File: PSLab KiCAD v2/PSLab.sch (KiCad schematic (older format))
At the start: 69 parts, among them CON1 USB-MINI-B, P10 Analog, P12 5V, P13 MCLR, P2 PROG, P3 DIO, P4 V+/V-, P5 sen-cap, P6 I2C, P7 NRF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

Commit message: Merged with Upstream to fix conflicts
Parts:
- added Q2: MMBT3904, TO_SOT_Packages_SMD:SOT-23, symbol MMBT3904
- added Q3: MMBT3906, TO_SOT_Packages_SMD:SOT-23, symbol MMBT3906
- R11, R5: value 200 -> 1K
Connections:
- wire segments 216 -> 228
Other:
- moved on the sheet: D1, D2, R11, R5
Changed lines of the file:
@@
 L R-RESCUE-proto1 R5
 U 1 1 55BABAB3
-P 10450 3000
-F 0 "R5" V 10530 3000 40  0000 C CNN
-F 1 "200" V 10457 3001 40  0000 C CNN
-F 2 "MyLib:R_0805" V 10380 3000 30  0001 C CNN
-F 3 "" H 10450 3000 30  0000 C CNN
-	1    10450 3000
-	0    1    -1   0
+P 10350 2920
+F 0 "R5" V 10430 2920 40  0000 C CNN
+F 1 "1K" V 10357 2921 40  0000 C CNN
+F 2 "MyLib:R_0805" V 10280 2920 30  0001 C CNN
+F 3 "" H 10350 2920 30  0000 C CNN
+	1    10350 2920
+	1    0    0    1
 $EndComp
 $Comp
 L R-RESCUE-proto1 R11
 U 1 1 55BABE2E
-P 10450 4000
-F 0 "R11" V 10530 4000 40  0000 C CNN
-F 1 "200" V 10457 4001 40  0000 C CNN
-F 2 "MyLib:R_0805" V 10380 4000 30  0001 C CNN
-F 3 "" H 10450 4000 30  0000 C CNN
-	1    10450 4000
-	0    1    -1   0
+P 10350 4285
+F 0 "R11" V 10430 4285 40  0000 C CNN
+F 1 "1K" V 10357 4286 40  0000 C CNN
+F 2 "MyLib:R_0805" V 10280 4285 30  0001 C CNN
+F 3 "" H 10350 4285 30  0000 C CNN
+	1    10350 4285
+	1    0    0    1
 $EndComp
 $Comp
 L ZENERsmall-RESCUE-proto1 D1
 U 1 1 55BABFCA
-P 10600 3225
-F 0 "D1" H 10600 3325 40  0000 C CNN
-F 1 "5V6" H 10600 3125 30  0000 C CNN
-F 2 "DIODE:Diode-MiniMELF_Standard" H 10600 3225 60  0001 C CNN
-F 3 "" H 10600 3225 60  0000 C CNN
-	1    10600 3225
-	1    0    0    -1
+P 10550 3360
+F 0 "D1" H 10550 3460 40  0000 C CNN
+F 1 "5V6" H 10550 3260 30  0000 C CNN
+F 2 "DIODE:Diode-MiniMELF_Standard" H 10550 3360 60  0001 C CNN
+F 3 "" H 10550 3360 60  0000 C CNN
+	1    10550 3360
+	0    -1   -1   0
 $EndComp
 $Comp
 L GND-RESCUE-proto1 #PWR046
 U 1 1 55BAC428
-P 10500 3225
-F 0 "#PWR046" H 10500 3225 30  0001 C CNN
-F 1 "GND" H 10500 3155 30  0001 C CNN
-F 2 "" H 10500 3225 60  0000 C CNN
-F 3 "" H 10500 3225 60  0000 C CNN
-	1    10500 3225
-	0    1    1    0
+P 10550 3535
+F 0 "#PWR046" H 10550 3535 30  0001 C CNN
+F 1 "GND" H 10550 3465 30  0001 C CNN
+F 2 "" H 10550 3535 60  0000 C CNN
+F 3 "" H 10550 3535 60  0000 C CNN
+	1    10550 3535
+	1    0    0    -1
 $EndComp
 $Comp
 L ZENERsmall-RESCUE-proto1 D2
 U 1 1 55BACB8F
-P 10600 3750
-F 0 "D2" H 10600 3850 40  0000 C CNN
-F 1 "5V6" H 10600 3650 30  0000 C CNN
-F 2 "DIODE:Diode-MiniMELF_Standard" H 10600 3750 60  0001 C CNN
-F 3 "" H 10600 3750 60  0000 C CNN
-	1    10600 3750
-	-1   0    0    1
+P 10550 3845
+F 0 "D2" H 10550 3945 40  0000 C CNN
+F 1 "5V6" H 10550 3745 30  0000 C CNN
+F 2 "DIODE:Diode-MiniMELF_Standard" H 10550 3845 60  0001 C CNN
+F 3 "" H 10550 3845 60  0000 C CNN
+	1    10550 3845
+	0    -1   -1   0
 $EndComp
 $Comp
 L GND-RESCUE-proto1 #PWR047
 U 1 1 55BACCF3
-P 10500 3750
-F 0 "#PWR047" H 10500 3750 30  0001 C CNN
-F 1 "GND" H 10500 3680 30  0001 C CNN
-F 2 "" H 10500 3750 60  0000 C CNN
-F 3 "" H 10500 3750 60  0000 C CNN
-	1    10500 3750
-	0    1    1    0
-$EndComp
-Text GLabel 10850 4000 2    60   Input ~ 0
+P 10550 3690
+F 0 "#PWR047" H 10550 3690 30  0001 C CNN
+F 1 "GND" H 10550 3620 30  0001 C CNN
+F 2 "" H 10550 3690 60  0000 C CNN
+F 3 "" H 10550 3690 60  0000 C CNN
+	1    10550 3690
+	-1   0    0    1
+$EndComp
+Text GLabel 10875 4705 2    60   Input ~ 0
 VR-
-Text GLabel 10850 3000 2    60   Input ~ 0
+Text GLabel 10885 2580 2    60   Input ~ 0
 VR+
 Text GLabel 4550 7175 0    40   Input ~ 0
@@
 L PWR_FLAG #FLG049
 U 1 1 55BC0DD9
-P 10700 3000
-F 0 "#FLG049" H 10700 3095 30  0001 C CNN
-F 1 "PWR_FLAG" H 10700 3180 30  0000 C CNN
-F 2 "" H 10700 3000 60  0000 C CNN
-F 3 "" H 10700 3000 60  0000 C CNN
-	1    10700 3000
+P 10815 2480
+F 0 "#FLG049" H 10815 2575 30  0001 C CNN
+F 1 "PWR_FLAG" H 10815 2660 30  0000 C CNN
+F 2 "" H 10815 2480 60  0000 C CNN
+F 3 "" H 10815 2480 60  0000 C CNN
+	1    10815 2480
 	1    0    0    -1
 $EndComp
@@
 L PWR_FLAG #FLG050
 U 1 1 55BC113E
-P 10700 4000
-F 0 "#FLG050" H 10700 4095 30  0001 C CNN
-F 1 "PWR_FLAG" H 10700 4180 30  0000 C CNN
-F 2 "" H 10700 4000 60  0000 C CNN
-F 3 "" H 10700 4000 60  0000 C CNN
-	1    10700 4000
+P 10795 4745
+F 0 "#FLG050" H 10795 4840 30  0001 C CNN
+F 1 "PWR_FLAG" H 10795 4925 30  0000 C CNN
+F 2 "" H 10795 4745 60  0000 C CNN
+F 3 "" H 10795 4745 60  0000 C CNN
+	1    10795 4745
 	-1   0    0    1
 $EndComp
@@
 Wire Wire Line
 	6250 4100 7050 4100
-Wire Wire Line
-	10200 3000 9925 3000
 Connection ~ 9925 3000
-Wire Wire Line
-	10200 4000 9925 4000
 Connection ~ 9925 4000
-Wire Wire Line
-	10700 3000 10850 3000
-Wire Wire Line
-	10700 3000 10700 3225
-Wire Wire Line
-	10700 3750 10700 4000
-Wire Wire Line
-	10700 4000 10850 4000
 Wire Wire Line
 	8025 2900 8025 3325
@@
 Wire Wire Line
 	1600 2575 1425 2575
+$Comp
+L MMBT3904 Q2
+U 1 1 593925C9
+P 10550 2680
+F 0 "Q2" V 10775 2515 50  0000 L CNN
+F 1 "MMBT3904" V 10770 2670 50  0000 L CNN
+F 2 "TO_SOT_Packages_SMD:SOT-23" H 10750 2605 50  0001 L CIN
+F 3 "" H 10550 2680 50  0001 L CNN
+	1    10550 2680
+	0    -1   -1   0
+$EndComp
+Wire Wire Line
+	10815 2480 10815 2580
+Wire Wire Line
+	10750 2580 10885 2580
+Connection ~ 10815 2580
+Wire Wire Line
+	10350 2670 10350 2580
+Wire Wire Line
+	10350 2580 10235 2580
+Wire Wire Line
+	10235 2580 10235 3000
+Wire Wire Line
+	10235 3000 9925 3000
+Wire Wire Line
+	10550 2880 10550 3260
+Wire Wire Line
+	10550 3535 10550 3460
+Connection ~ 10550 3240
+Wire Wire Line
+	10350 3170 10350 3240
+Wire Wire Line
+	10350 3240 10550 3240
+Wire Wire Line
+	10550 3745 10550 3690
+Wire Wire Line
+	10350 4035 10350 3995
+Wire Wire Line
+	10350 3995 10550 3995
+Wire Wire Line
+	10550 3945 10550 4405
+$Comp
+L MMBT3906 Q3
+U 1 1 5939854E
+P 10550 4605
+F 0 "Q3" V 10795 4445 50  0000 L CNN
+F 1 "MMBT3906" V 10795 4605 50  0000 L CNN
+F 2 "TO_SOT_Packages_SMD:SOT-23" H 10750 4530 50  0001 L CIN
+F 3 "" H 10550 4605 50  0001 L CNN
+	1    10550 4605
+	0    -1   1    0
+$EndComp
+Wire Wire Line
+	10350 4705 10350 4705
+Wire Wire Line
+	10350 4705 10350 4535
+Connection ~ 10550 3995
+Wire Wire Line
+	10750 4705 10875 4705
+Wire Wire Line
+	10795 4745 10795 4705
+Connection ~ 10795 4705
 $EndSCHEMATC

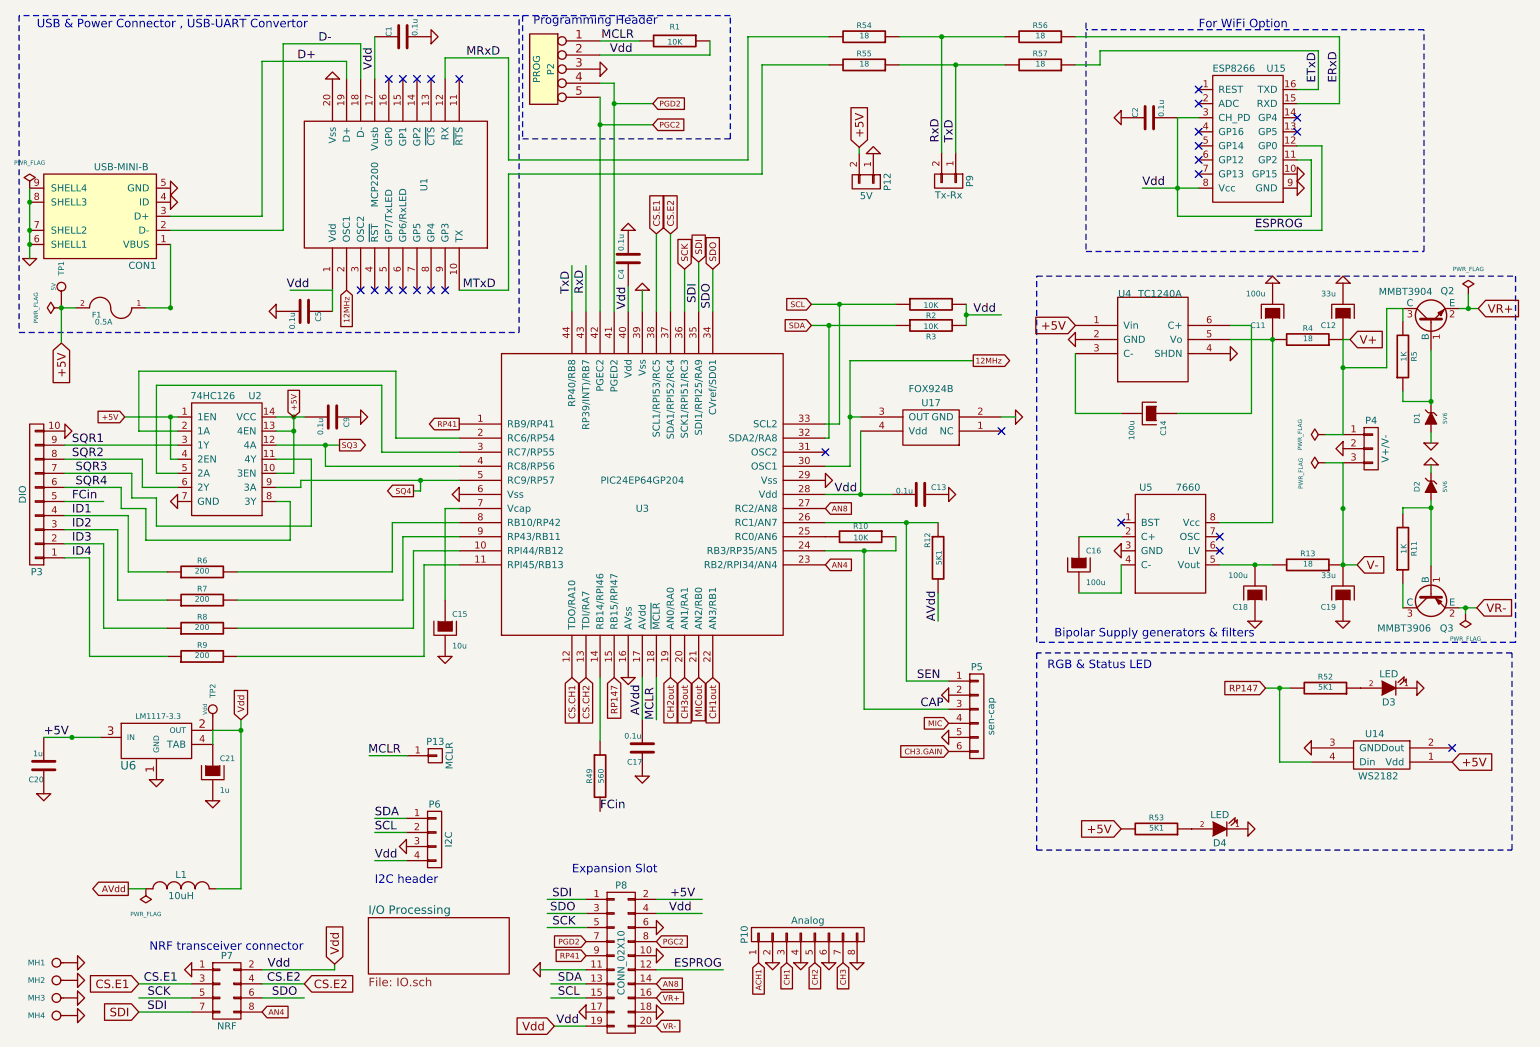
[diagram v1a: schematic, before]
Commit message: Assigned footprints to components
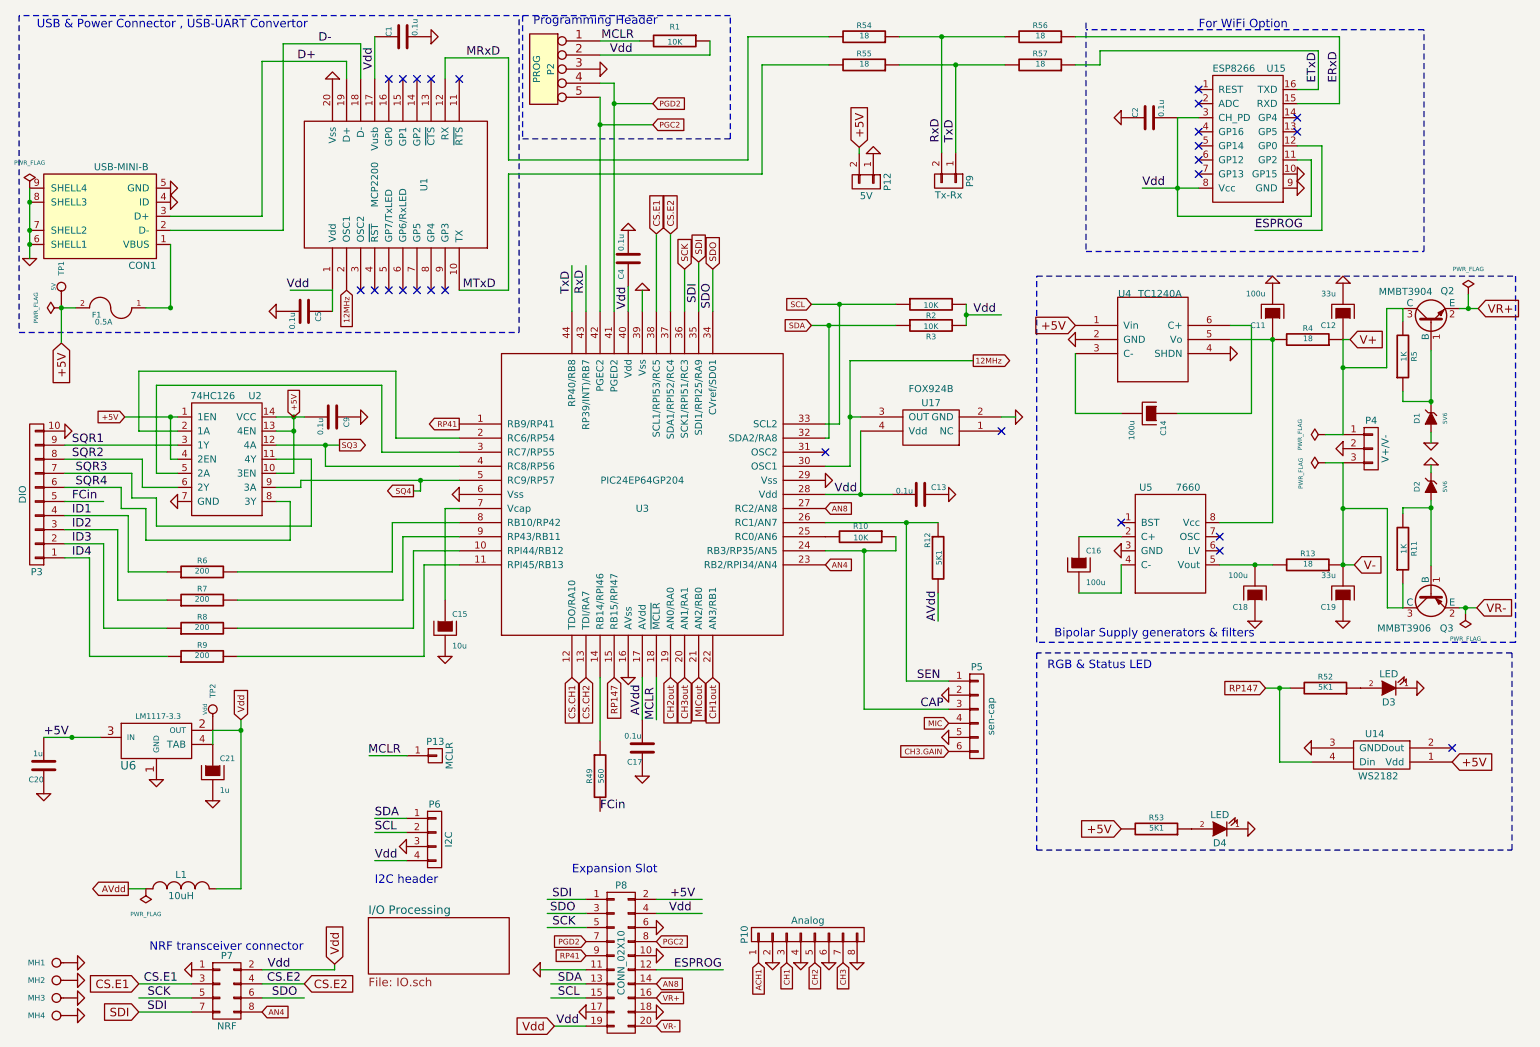
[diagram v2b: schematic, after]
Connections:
- wire segments 228 -> 261
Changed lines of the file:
@@
 Text GLabel 8025 2700 0    60   Input ~ 0
 +5V
-Text GLabel 10025 4400 2    60   Input ~ 0
+Text GLabel 10005 4400 2    60   Input ~ 0
 V-
 Text GLabel 9975 2800 2    60   Input ~ 0
@@
 	825  2575 925  2575
 Wire Wire Line
-	700  5625 1100 5625
+	700  5625 900  5625
+Wire Wire Line
+	900  5625 1100 5625
 Connection ~ 825  2575
 Wire Wire Line
@@
 	5150 2600 5150 2050
 Wire Wire Line
-	6250 3900 6725 3900
+	6250 3900 6500 3900
+Wire Wire Line
+	6500 3900 6725 3900
 Wire Wire Line
 	6250 3400 6350 3400
@@
 	3550 800  4000 800
 Wire Wire Line
-	4750 980  4750 2600
+	4750 980  4750 1125
+Wire Wire Line
+	4750 1125 4750 2600
 Wire Wire Line
 	4750 980  4650 980
 Wire Wire Line
-	4650 1080 4650 2600
+	4650 1080 4650 1275
+Wire Wire Line
+	4650 1275 4650 2600
 Wire Wire Line
 	4650 680  4930 680
@@
 	3050 950  3050 650
 Wire Wire Line
-	6150 2700 6750 2700
+	6150 2700 6275 2700
+Wire Wire Line
+	6275 2700 6750 2700
 Connection ~ 6275 2700
 Wire Wire Line
-	6150 2550 6750 2550
+	6150 2550 6350 2550
+Wire Wire Line
+	6350 2550 6750 2550
 Connection ~ 6350 2550
 Wire Wire Line
-	7250 2550 7250 2700
+	7250 2550 7250 2625
+Wire Wire Line
+	7250 2625 7250 2700
 Wire Wire Line
 	7250 2625 7500 2625
@@
 	9925 2800 9975 2800
 Wire Wire Line
-	9925 2800 9925 3475
-Wire Wire Line
-	9925 3675 9925 4400
-Wire Wire Line
-	9050 4400 9425 4400
-Wire Wire Line
-	9925 4400 10025 4400
+	9925 2800 9925 3000
+Wire Wire Line
+	9925 3000 9925 3475
+Wire Wire Line
+	9925 3675 9925 4000
+Wire Wire Line
+	9925 4000 9925 4400
+Wire Wire Line
+	9050 4400 9300 4400
+Wire Wire Line
+	9300 4400 9425 4400
+Wire Wire Line
+	9925 4400 10005 4400
 Connection ~ 9925 4400
 Wire Wire Line
 	8900 1225 8750 1225
 Wire Wire Line
-	8500 1725 8900 1725
+	8500 1725 8750 1725
+Wire Wire Line
+	8750 1725 8900 1725
 Connection ~ 8750 1725
 Wire Wire Line
@@
 	2400 2025 1600 2025
 Wire Wire Line
-	600  1725 600  2225
+	600  1725 600  1825
+Wire Wire Line
+	600  1825 600  2025
+Wire Wire Line
+	600  2025 600  2125
+Wire Wire Line
+	600  2125 600  2225
 Connection ~ 600  2025
 Connection ~ 600  1825
@@
 	2700 3700 2700 3550
 Wire Wire Line
-	2350 3550 2800 3550
+	2350 3550 2700 3550
+Wire Wire Line
+	2700 3550 2800 3550
 Wire Wire Line
 	2350 3650 2600 3650
@@
 	3175 4450 2075 4450
 Wire Wire Line
-	2525 3800 3650 3800
+	2525 3800 3375 3800
+Wire Wire Line
+	3375 3800 3650 3800
 Wire Wire Line
 	3100 3600 3100 3125
@@
 	850  3750 1325 3750
 Wire Wire Line
-	2350 3350 2550 3350
+	2350 3350 2475 3350
+Wire Wire Line
+	2475 3350 2550 3350
 Wire Wire Line
 	1650 3650 1600 3650
@@
 	1600 3650 1600 3350
 Wire Wire Line
-	1275 3350 1650 3350
+	1275 3350 1600 3350
+Wire Wire Line
+	1600 3350 1650 3350
 Wire Wire Line
 	850  3850 1250 3850
@@
 	2475 3750 2350 3750
 Wire Wire Line
-	2475 3350 2475 3750
+	2475 3350 2475 3450
+Wire Wire Line
+	2475 3450 2475 3750
 Connection ~ 2475 3350
 Wire Wire Line
@@
 	5050 6875 5375 6875
 Wire Wire Line
-	8750 1225 8750 1925
+	8750 1225 8750 1725
+Wire Wire Line
+	8750 1725 8750 1925
 Wire Wire Line
 	9600 1525 9700 1525
@@
 	1900 5575 2100 5575
 Wire Wire Line
-	2100 5500 2100 6700
+	2100 5500 2100 5575
+Wire Wire Line
+	2100 5575 2100 6700
 Wire Wire Line
 	6825 5225 7125 5225
@@
 	6525 4300 6525 5425
 Wire Wire Line
-	6250 4300 6750 4300
-Wire Wire Line
-	6250 4100 7050 4100
+	6250 4300 6525 4300
+Wire Wire Line
+	6525 4300 6750 4300
+Wire Wire Line
+	6250 4100 6825 4100
+Wire Wire Line
+	6825 4100 7050 4100
 Connection ~ 9925 3000
 Connection ~ 9925 4000
@@
 	5050 7275 5525 7275
 Wire Wire Line
-	9375 5275 9550 5275
+	9375 5275 9475 5275
+Wire Wire Line
+	9475 5275 9550 5275
 Wire Wire Line
 	9700 5800 9475 5800
@@
 	5700 650  6275 650
 Wire Wire Line
-	6775 650  7525 650
+	6775 650  7075 650
+Wire Wire Line
+	7075 650  7525 650
 Wire Wire Line
 	7075 1475 7075 650
 Connection ~ 7075 650
 Wire Wire Line
-	6775 850  7525 850
+	6775 850  7175 850
+Wire Wire Line
+	7175 850  7525 850
 Connection ~ 7175 850
 Wire Wire Line
@@
 	7300 2950 6425 2950
 Wire Wire Line
-	6425 2950 6425 3700
+	6425 2950 6425 3350
+Wire Wire Line
+	6425 3350 6425 3700
 $Comp
 L FOX924B U17
@@
 	10815 2480 10815 2580
 Wire Wire Line
-	10750 2580 10885 2580
+	10750 2580 10815 2580
+Wire Wire Line
+	10815 2580 10885 2580
 Connection ~ 10815 2580
 Wire Wire Line
@@
 	10235 3000 9925 3000
 Wire Wire Line
-	10550 2880 10550 3260
+	10550 2880 10550 3240
+Wire Wire Line
+	10550 3240 10550 3260
 Wire Wire Line
 	10550 3535 10550 3460
@@
 	10350 3995 10550 3995
 Wire Wire Line
-	10550 3945 10550 4405
+	10550 3945 10550 3995
+Wire Wire Line
+	10550 3995 10550 4405
 $Comp
 L MMBT3906 Q3
@@
 $EndComp
 Wire Wire Line
-	10350 4705 10350 4705
+	10240 4705 10350 4705
 Wire Wire Line
 	10350 4705 10350 4535
 Connection ~ 10550 3995
 Wire Wire Line
-	10750 4705 10875 4705
+	10750 4705 10795 4705
+Wire Wire Line
+	10795 4705 10875 4705
 Wire Wire Line
 	10795 4745 10795 4705
 Connection ~ 10795 4705
+Wire Wire Line
+	9925 4000 10240 4000
+Wire Wire Line
+	10240 4000 10240 4705
 $EndSCHEMATC

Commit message: Fix #16 : PCB Layout for Voltage Regulator
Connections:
- wire segments 261 -> 230
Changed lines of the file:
@@
 	825  2575 925  2575
 Wire Wire Line
-	700  5625 900  5625
-Wire Wire Line
-	900  5625 1100 5625
+	700  5625 1100 5625
 Connection ~ 825  2575
 Wire Wire Line
@@
 	5150 2600 5150 2050
 Wire Wire Line
-	6250 3900 6500 3900
-Wire Wire Line
-	6500 3900 6725 3900
+	6250 3900 6725 3900
 Wire Wire Line
 	6250 3400 6350 3400
@@
 	3550 800  4000 800
 Wire Wire Line
-	4750 980  4750 1125
-Wire Wire Line
-	4750 1125 4750 2600
+	4750 980  4750 2600
 Wire Wire Line
 	4750 980  4650 980
 Wire Wire Line
-	4650 1080 4650 1275
-Wire Wire Line
-	4650 1275 4650 2600
+	4650 1080 4650 2600
 Wire Wire Line
 	4650 680  4930 680
@@
 	3050 950  3050 650
 Wire Wire Line
-	6150 2700 6275 2700
-Wire Wire Line
-	6275 2700 6750 2700
+	6150 2700 6750 2700
 Connection ~ 6275 2700
 Wire Wire Line
-	6150 2550 6350 2550
-Wire Wire Line
-	6350 2550 6750 2550
+	6150 2550 6750 2550
 Connection ~ 6350 2550
 Wire Wire Line
-	7250 2550 7250 2625
-Wire Wire Line
-	7250 2625 7250 2700
+	7250 2550 7250 2700
 Wire Wire Line
 	7250 2625 7500 2625
@@
 	9925 2800 9975 2800
 Wire Wire Line
-	9925 2800 9925 3000
-Wire Wire Line
-	9925 3000 9925 3475
-Wire Wire Line
-	9925 3675 9925 4000
-Wire Wire Line
-	9925 4000 9925 4400
-Wire Wire Line
-	9050 4400 9300 4400
-Wire Wire Line
-	9300 4400 9425 4400
+	9925 2800 9925 3475
+Wire Wire Line
+	9925 3675 9925 4400
+Wire Wire Line
+	9050 4400 9425 4400
 Wire Wire Line
 	9925 4400 10005 4400
@@
 	8900 1225 8750 1225
 Wire Wire Line
-	8500 1725 8750 1725
-Wire Wire Line
-	8750 1725 8900 1725
+	8500 1725 8900 1725
 Connection ~ 8750 1725
 Wire Wire Line
@@
 	2400 2025 1600 2025
 Wire Wire Line
-	600  1725 600  1825
-Wire Wire Line
-	600  1825 600  2025
-Wire Wire Line
-	600  2025 600  2125
-Wire Wire Line
-	600  2125 600  2225
+	600  1725 600  2225
 Connection ~ 600  2025
 Connection ~ 600  1825
@@
 	2700 3700 2700 3550
 Wire Wire Line
-	2350 3550 2700 3550
-Wire Wire Line
-	2700 3550 2800 3550
+	2350 3550 2800 3550
 Wire Wire Line
 	2350 3650 2600 3650
@@
 	3175 4450 2075 4450
 Wire Wire Line
-	2525 3800 3375 3800
-Wire Wire Line
-	3375 3800 3650 3800
+	2525 3800 3650 3800
 Wire Wire Line
 	3100 3600 3100 3125
@@
 	850  3750 1325 3750
 Wire Wire Line
-	2350 3350 2475 3350
-Wire Wire Line
-	2475 3350 2550 3350
+	2350 3350 2550 3350
 Wire Wire Line
 	1650 3650 1600 3650
@@
 	1600 3650 1600 3350
 Wire Wire Line
-	1275 3350 1600 3350
-Wire Wire Line
-	1600 3350 1650 3350
+	1275 3350 1650 3350
 Wire Wire Line
 	850  3850 1250 3850
@@
 	2475 3750 2350 3750
 Wire Wire Line
-	2475 3350 2475 3450
-Wire Wire Line
-	2475 3450 2475 3750
+	2475 3350 2475 3750
 Connection ~ 2475 3350
 Wire Wire Line
@@
 	5050 6875 5375 6875
 Wire Wire Line
-	8750 1225 8750 1725
-Wire Wire Line
-	8750 1725 8750 1925
+	8750 1225 8750 1925
 Wire Wire Line
 	9600 1525 9700 1525
@@
 	1900 5575 2100 5575
 Wire Wire Line
-	2100 5500 2100 5575
-Wire Wire Line
-	2100 5575 2100 6700
+	2100 5500 2100 6700
 Wire Wire Line
 	6825 5225 7125 5225
@@
 	6525 4300 6525 5425
 Wire Wire Line
-	6250 4300 6525 4300
-Wire Wire Line
-	6525 4300 6750 4300
-Wire Wire Line
-	6250 4100 6825 4100
-Wire Wire Line
-	6825 4100 7050 4100
+	6250 4300 6750 4300
+Wire Wire Line
+	6250 4100 7050 4100
 Connection ~ 9925 3000
 Connection ~ 9925 4000
@@
 	5050 7275 5525 7275
 Wire Wire Line
-	9375 5275 9475 5275
-Wire Wire Line
-	9475 5275 9550 5275
+	9375 5275 9550 5275
 Wire Wire Line
 	9700 5800 9475 5800
@@
 	5700 650  6275 650
 Wire Wire Line
-	6775 650  7075 650
-Wire Wire Line
-	7075 650  7525 650
+	6775 650  7525 650
 Wire Wire Line
 	7075 1475 7075 650
 Connection ~ 7075 650
 Wire Wire Line
-	6775 850  7175 850
-Wire Wire Line
-	7175 850  7525 850
+	6775 850  7525 850
 Connection ~ 7175 850
 Wire Wire Line
@@
 	7300 2950 6425 2950
 Wire Wire Line
-	6425 2950 6425 3350
-Wire Wire Line
-	6425 3350 6425 3700
+	6425 2950 6425 3700
 $Comp
 L FOX924B U17
@@
 	10815 2480 10815 2580
 Wire Wire Line
-	10750 2580 10815 2580
-Wire Wire Line
-	10815 2580 10885 2580
+	10750 2580 10885 2580
 Connection ~ 10815 2580
 Wire Wire Line
@@
 	10235 3000 9925 3000
 Wire Wire Line
-	10550 2880 10550 3240
-Wire Wire Line
-	10550 3240 10550 3260
+	10550 2880 10550 3260
 Wire Wire Line
 	10550 3535 10550 3460
@@
 	10350 3995 10550 3995
 Wire Wire Line
-	10550 3945 10550 3995
-Wire Wire Line
-	10550 3995 10550 4405
+	10550 3945 10550 4405
 $Comp
 L MMBT3906 Q3
@@
 Connection ~ 10550 3995
 Wire Wire Line
-	10750 4705 10795 4705
-Wire Wire Line
-	10795 4705 10875 4705
+	10750 4705 10875 4705
 Wire Wire Line
 	10795 4745 10795 4705
